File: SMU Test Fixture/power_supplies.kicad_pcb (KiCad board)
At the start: 2 copper layers, 85.1 x 130.1 mm, 42 parts, among them J13 Hot_Spade, J14 Power Outputs, J15 Neutral_Spade, T1 VPP28-1060, U10 LT3045, U11 LT1086-12, U12 LT3094, U9 LT1086-5.0

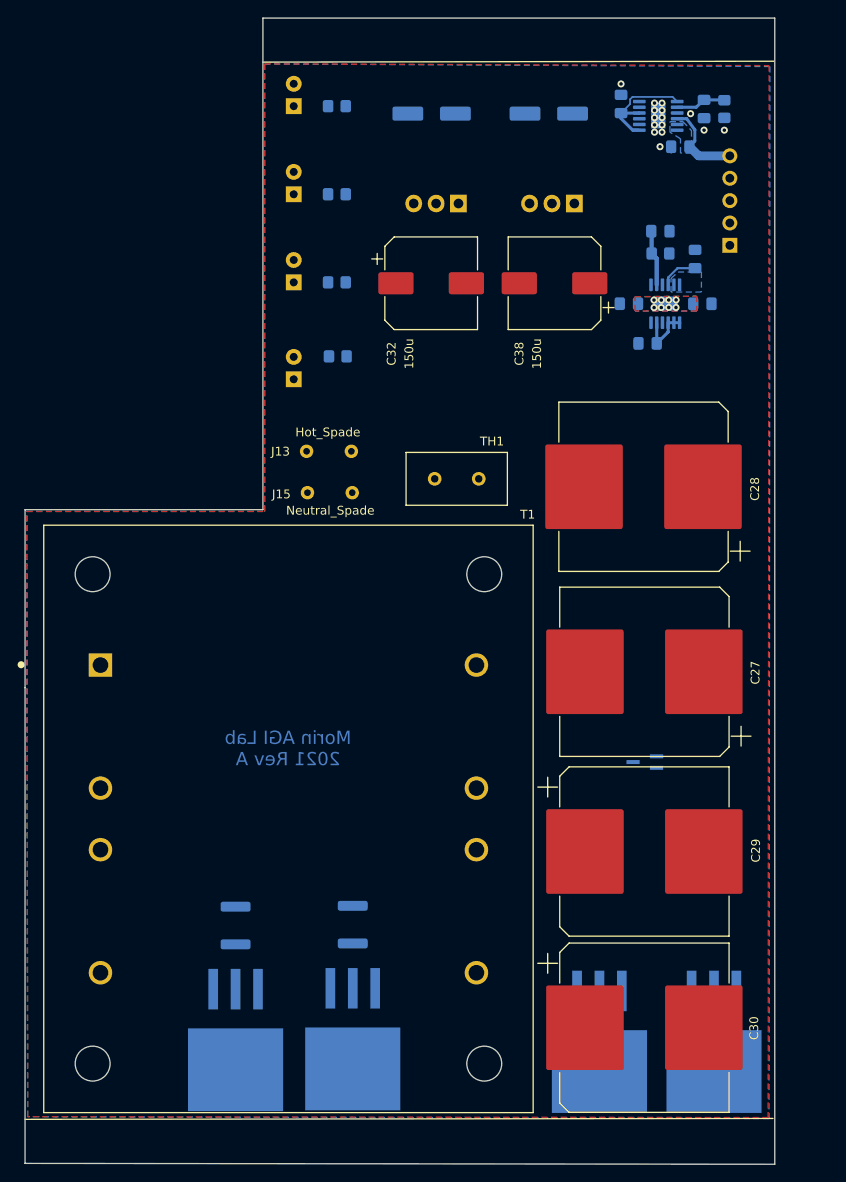
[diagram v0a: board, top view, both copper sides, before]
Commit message: Begin routing traces.
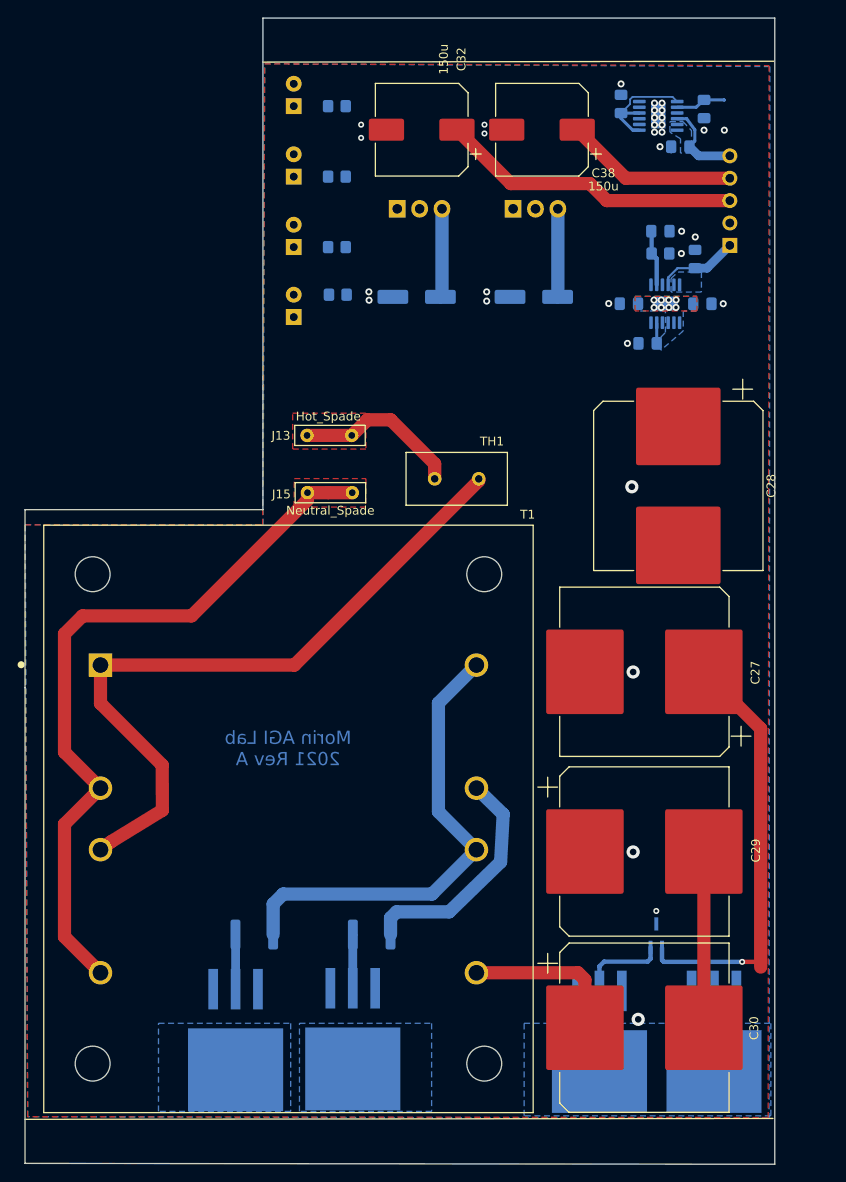
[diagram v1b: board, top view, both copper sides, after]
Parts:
- removed R37: 150k, Resistor_SMD:R_0805_2012Metric_Pad1.20x1.40mm_HandSolder
- U10: value LT3045 -> MAGI_Symbols_LT3045xMSE-1
- U12: value LT3094 -> LT3094xMSE
- moved C37 25.6 mm to (148.3, 60.5), turned to 180 degrees
- moved C31 23.8 mm to (161.6, 60.5), turned to 180 degrees
- moved U9 20.1 mm to (146.1, 50.5), turned to 0 degrees
- moved D39 19.7 mm to (175.5, 133.1), turned to 90 degrees
- moved C38 17.5 mm to (162.5, 41.6)
- moved C32 17.5 mm to (148.9, 41.6), turned to 180 degrees
- moved D43 7.06 mm to (134.3, 62.8)
- moved R34 7.00 mm to (139.3, 60.3)
- moved U11 6.23 mm to (159.2, 50.5), turned to 0 degrees
- moved D44 4.00 mm to (134.3, 54.9)
- moved R35 4.00 mm to (139.2, 54.9)
- moved C28 3.95 mm to (178.0, 82.0), turned to 270 degrees
- moved F2 2.43 mm to (143.2, 132.9), turned to 0 degrees
- moved F1 2.36 mm to (129.9, 132.9), turned to 0 degrees
- moved D45 2.00 mm to (134.3, 46.9)
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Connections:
- U10 pad 13: (no net) -> GND
- U10 pad 2: (no net) -> /unreg_pos_18VDC
- U10 pad 4: /unreg_pos_18VDC -> (no net)
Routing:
- net Net-(J15-Pad1): track 0.00 -> 83.3 mm
- net Net-(T1-Pad1): track 0.00 -> 79.5 mm
- net /unreg_pos_18VDC: track 13.0 -> 82.4 mm, vias 0 -> 1
- net Net-(F1-Pad2): track 0.00 -> 53.6 mm
- net +5V: track 0.00 -> 34.3 mm
- net Net-(F2-Pad2): track 0.00 -> 26.6 mm
- net /unreg_neg_18VDC: track 6.54 -> 32.6 mm
- net +12V: track 0.00 -> 19.6 mm
- net Net-(J13-Pad1): track 0.00 -> 19.0 mm
- net GND: track 0.26 -> 18.3 mm, vias 9 -> 33
- net Net-(D37-Pad2): track 0.00 -> 6.21 mm
- net Net-(D38-Pad2): track 0.00 -> 6.11 mm
- net -15V: track 4.32 -> 9.34 mm
- net (no net): vias 6 -> 0
- added copper zone on B.Cu, net Net-(D37-Pad2)
- added copper zone on B.Cu, net Net-(D38-Pad2)
- added copper zone on F.Cu, net Net-(J13-Pad1)
- added copper zone on F.Cu, net Net-(J15-Pad1)
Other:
- net class HV added: clearance 2, trace_width 1.5, via_dia 1.5, via_drill 0.75

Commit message: HV and rectification sections routed.
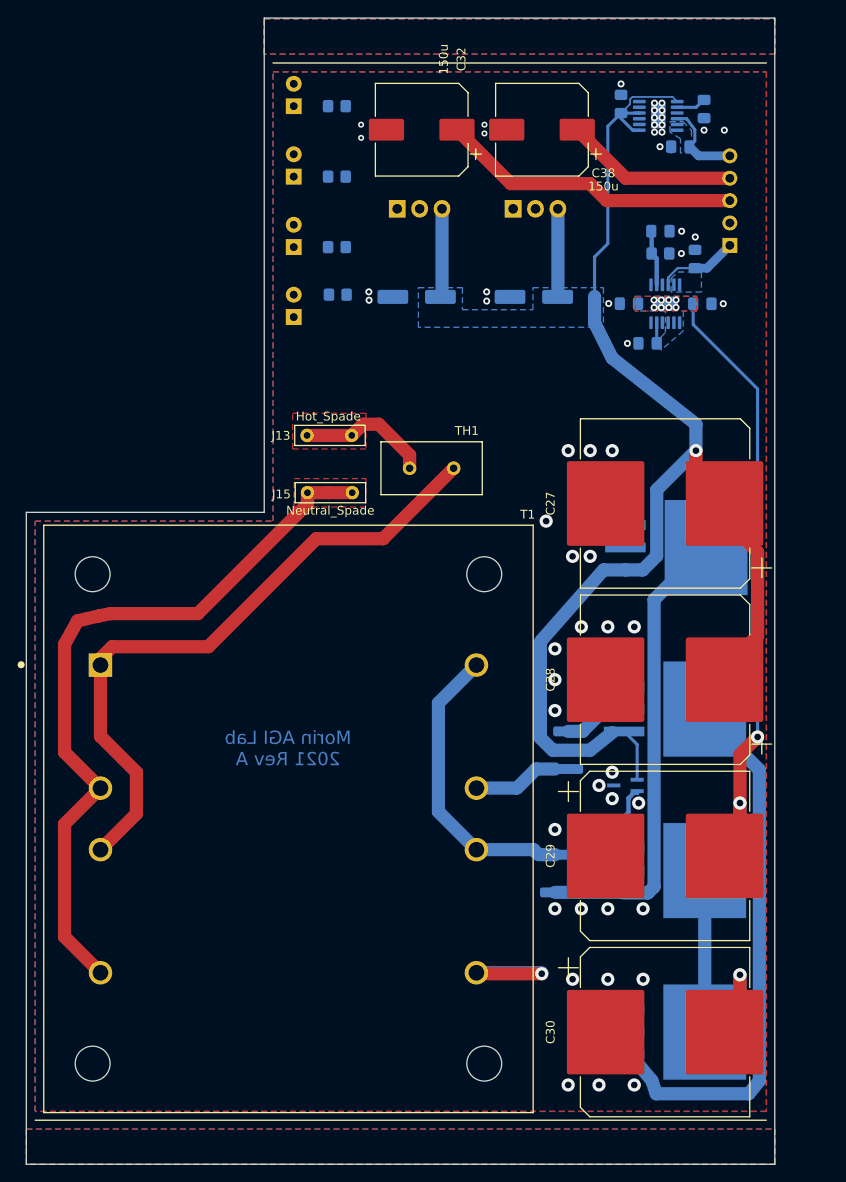
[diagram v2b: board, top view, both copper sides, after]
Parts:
- moved D37 75.0 mm to (177.8, 89.0), turned to 0 degrees
- moved D38 52.4 mm to (177.6, 107.3), turned to 0 degrees
- moved F1 34.8 mm to (164.0, 126.0), turned to 90 degrees
- moved F2 30.6 mm to (165.5, 112.0), turned to 270 degrees
- moved C28 22.1 mm to (176.5, 104.0), turned to 180 degrees
- moved D40 19.9 mm to (177.6, 125.7), turned to 0 degrees
- moved C27 19.2 mm to (176.5, 84.0)
- moved D39 17.4 mm to (172.0, 116.0), turned to 180 degrees
- moved D41 8.65 mm to (177.6, 144.0), turned to 0 degrees
- moved TH1 3.09 mm to (150.0, 80.0)
- moved C29 2.40 mm to (176.5, 124.0)
- moved C30 2.40 mm to (176.5, 144.0)
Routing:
- net /unreg_neg_18VDC: track 32.6 -> 125.3 mm, vias 8 -> 11
- net /unreg_pos_18VDC: track 82.4 -> 168.4 mm
- net Net-(D38-Pad2): track 6.11 -> 73.7 mm
- net Net-(D37-Pad2): track 6.21 -> 52.4 mm
- net Net-(F1-Pad2): track 53.6 -> 33.3 mm
- net Net-(F2-Pad2): track 26.6 -> 9.62 mm
- net Net-(T1-Pad1): track 79.5 -> 74.1 mm
- net Net-(J13-Pad1): track 19.0 -> 15.1 mm
- net GND: track 18.3 -> 15.1 mm, vias 33 -> 56
- net Net-(C35-Pad1): track 5.69 -> 3.38 mm
- added copper zone on B.Cu, net (none)
- added copper zone on F.Cu, net (none)
- added copper zone on B.Cu, net /unreg_pos_18VDC
- removed copper zone on B.Cu, net Net-(D37-Pad2)
- removed copper zone on B.Cu, net Net-(D38-Pad2)
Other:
- board size 85.1 x 130.1 mm -> 84.9 x 130.1 mm

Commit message: Finish routing low voltage side, silkscreen
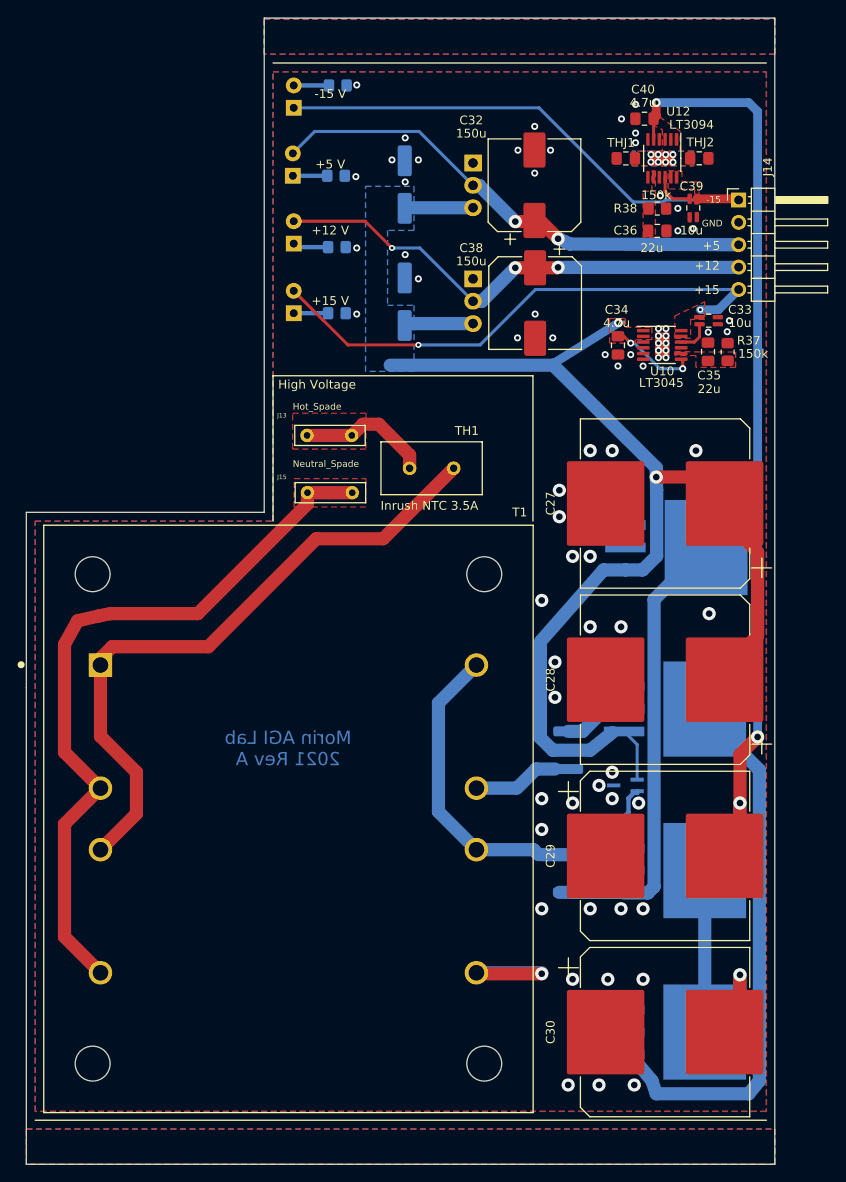
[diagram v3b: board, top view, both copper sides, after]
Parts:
- added R37: 150k, Resistor_SMD:R_0805_2012Metric_Pad1.20x1.40mm_HandSolder, F.Cu at (183.6, 66.8)
- C33, C39: footprint Capacitor_SMD:C_0805_2012Metric_Pad1.18x1.45mm_HandSolder -> MAGI_Footprints:C_0805_2012Metric_Pad1.18x1.45mm_HandSolder_Kelvin; moved to F.Cu
- C34, C35, C36, C40, J14, R38, THJ1, THJ2: moved to F.Cu
- TH1: value 3.5A max <130C -> Inrush NTC 3.5A
- U10: value MAGI_Symbols_LT3045xMSE-1 -> LT3045; moved to F.Cu
- U12: value LT3094xMSE -> LT3094; moved to F.Cu
- moved C35 27.6 mm to (181.4, 66.8), turned to 90 degrees
- moved C34 27.4 mm to (171.2, 66.0), turned to 270 degrees
- moved U10 26.0 mm to (176.2, 66.0)
- moved C40 25.5 mm to (174.2, 40.3)
- moved D43 23.8 mm to (134.3, 39.1)
- moved R34 23.8 mm to (139.3, 36.5)
- moved D42 23.5 mm to (134.3, 62.4)
- moved R33 23.5 mm to (139.2, 62.4)
- moved C33 20.0 mm to (181.4, 63.2), turned to 0 degrees
- moved C38 19.7 mm to (161.8, 61.2), turned to 270 degrees
- moved THJ2 16.5 mm to (180.4, 44.8)
- moved U12 16.5 mm to (176.2, 44.8), turned to 270 degrees
- moved THJ1 16.5 mm to (172.0, 44.8)
- moved C31 14.7 mm to (146.9, 61.1), turned to 90 degrees
- moved C32 14.3 mm to (161.7, 47.9), turned to 90 degrees
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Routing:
- net -15V: track 9.34 -> 64.5 mm
- net +15V: track 9.82 -> 64.7 mm, vias 0 -> 2
- net +12V: track 19.6 -> 55.9 mm, vias 0 -> 3
- net /unreg_neg_18VDC: track 125.3 -> 158.0 mm, vias 11 -> 12
- net +5V: track 34.3 -> 56.9 mm, vias 0 -> 2
- net Net-(C36-Pad2): track 6.30 -> 0.00 mm
- net /unreg_pos_18VDC: track 168.4 -> 162.3 mm, vias 1 -> 4
- net Net-(D43-Pad2): track 0.00 -> 4.00 mm
- net Net-(D45-Pad1): track 0.00 -> 3.90 mm
- net Net-(D44-Pad1): track 0.00 -> 3.90 mm
- net Net-(D42-Pad1): track 0.00 -> 3.90 mm
- net Net-(C35-Pad1): track 3.38 -> 0.00 mm
- net Net-(F1-Pad2): track 33.3 -> 35.8 mm
- net Net-(D37-Pad2): track 52.4 -> 51.9 mm
- net GND: track 15.1 -> 14.9 mm, vias 56 -> 73
- added copper zone on F.Cu, net +15V
- added copper zone on F.Cu, net -15V
- added copper zone on F.Cu, net /unreg_pos_18VDC
- added copper zone on F.Cu, net Net-(C35-Pad1)
- added copper zone on F.Cu, net Net-(C36-Pad2)
- removed copper zone on B.Cu, net +15V
- removed copper zone on B.Cu, net -15V
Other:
- board text added: "+12 V"
- board text added: "+15 V"
- board text added: "+5 V"
- board text added: "-15 V"
- board text added: "High Voltage"

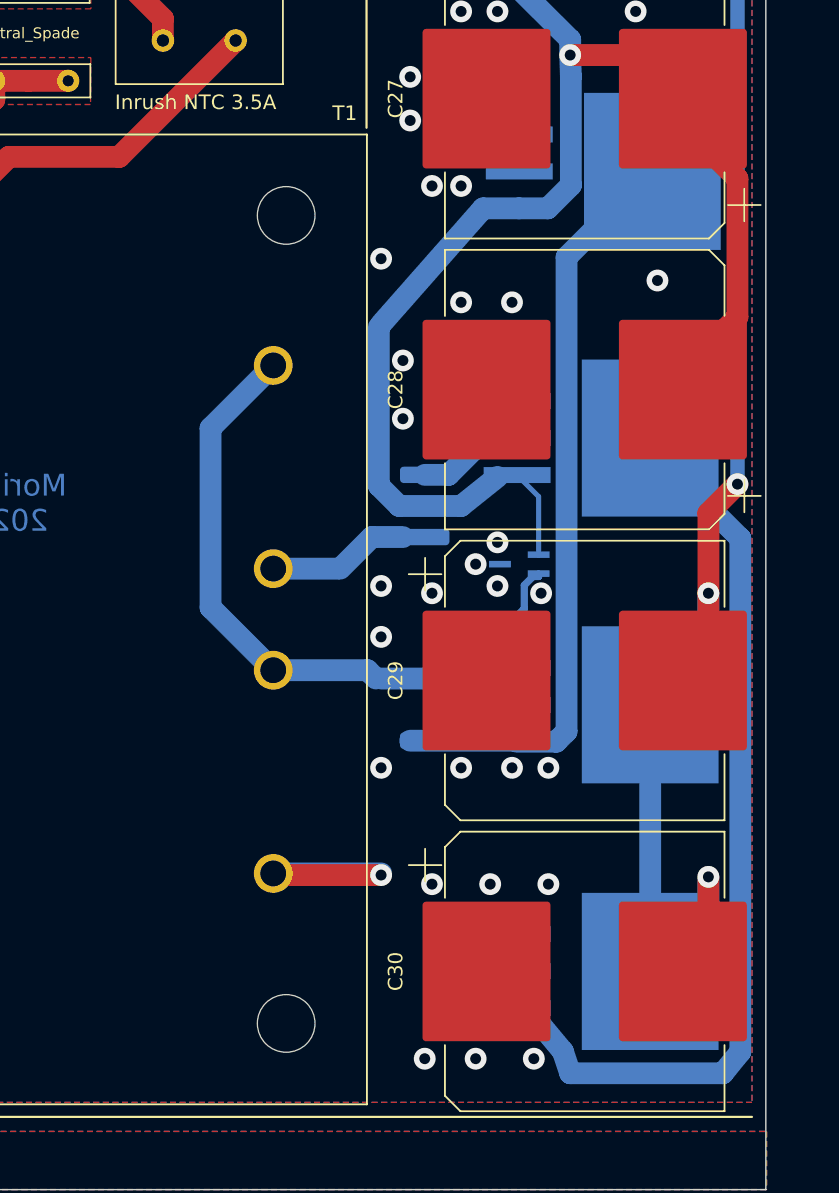
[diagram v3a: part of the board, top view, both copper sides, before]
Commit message: Add crowbar protection for regulator inputs.
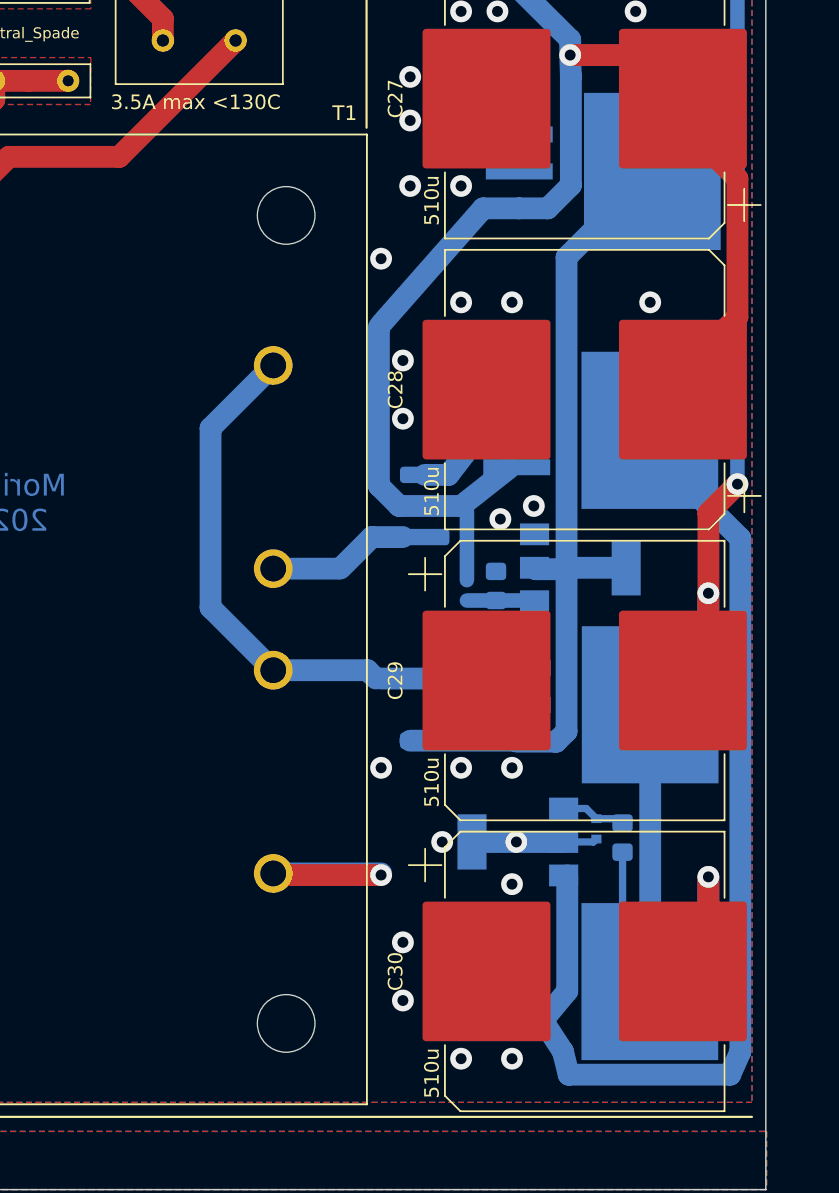
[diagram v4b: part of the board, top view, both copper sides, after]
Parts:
- added D46: 20V, Diode_SMD:D_SOD-523, B.Cu at (177.3, 134.2)
- added Q1: IRFL014, Package_TO_SOT_SMD:SOT-223, B.Cu at (171.9, 135.1)
- added Q2: IRFL014, Package_TO_SOT_SMD:SOT-223, B.Cu at (176.2, 116.2)
- added R39: 1K, Resistor_SMD:R_0805_2012Metric_Pad1.20x1.40mm_HandSolder, B.Cu at (179.1, 134.8)
- added R40: 1K, Resistor_SMD:R_0805_2012Metric_Pad1.20x1.40mm_HandSolder, B.Cu at (170.4, 117.5)
- D39: value 20V Clamp -> 20V; footprint Package_TO_SOT_SMD:SOT-323_SC-70_Handsoldering -> Diode_SMD:D_SOD-523
- TH1: value Inrush NTC 3.5A -> 3.5A max <130C
- moved D39 4.02 mm to (168.4, 117.8), turned to 270 degrees
- moved D41 0.70 mm to (177.6, 144.7)
- moved D38 0.53 mm to (177.6, 106.8)
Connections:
- net Net-(D37-Pad2) renamed /unfilt_pos
- net Net-(D38-Pad2) renamed /unfilt_neg
- D39 pad 2: /unreg_neg_18VDC -> Net-(D39-Pad2)
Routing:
- net /unfilt_neg: track 73.7 -> 88.5 mm
- net GND: track 14.9 -> 23.5 mm, vias 73 -> 68
- net /unfilt_pos: track 51.9 -> 58.3 mm
- net Net-(D39-Pad2): track 0.00 -> 4.67 mm
- net Net-(D46-Pad2): track 0.00 -> 4.46 mm
- net /unreg_neg_18VDC: track 158.0 -> 154.3 mm
